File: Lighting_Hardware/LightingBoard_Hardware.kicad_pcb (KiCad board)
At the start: 2 copper layers, 61 x 108.8 mm, 22 parts, among them U1 LDD-1500L, U2 LDD-1500L, U3 TM4C129E_Launchpad, U4 OKI

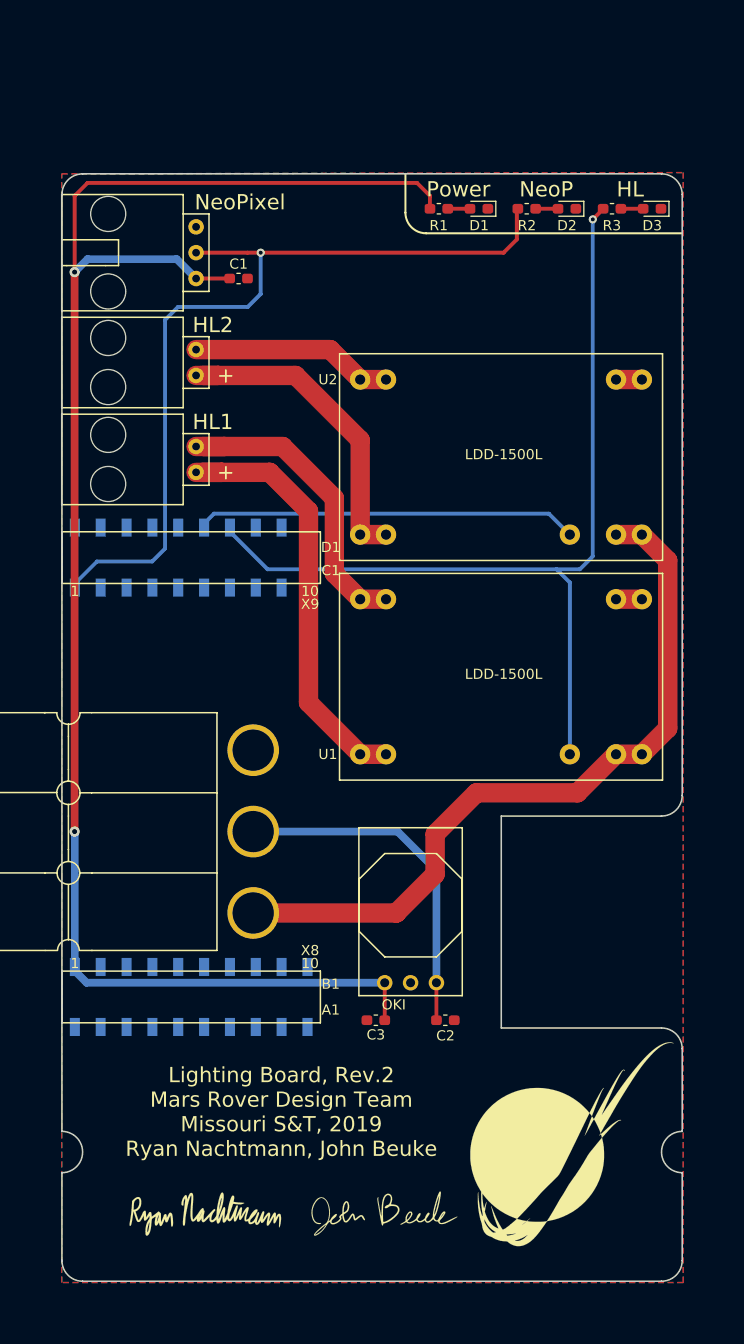
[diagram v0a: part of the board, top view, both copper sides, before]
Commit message: Added the NEW DC-DC Buck Converter for the NeoPixels
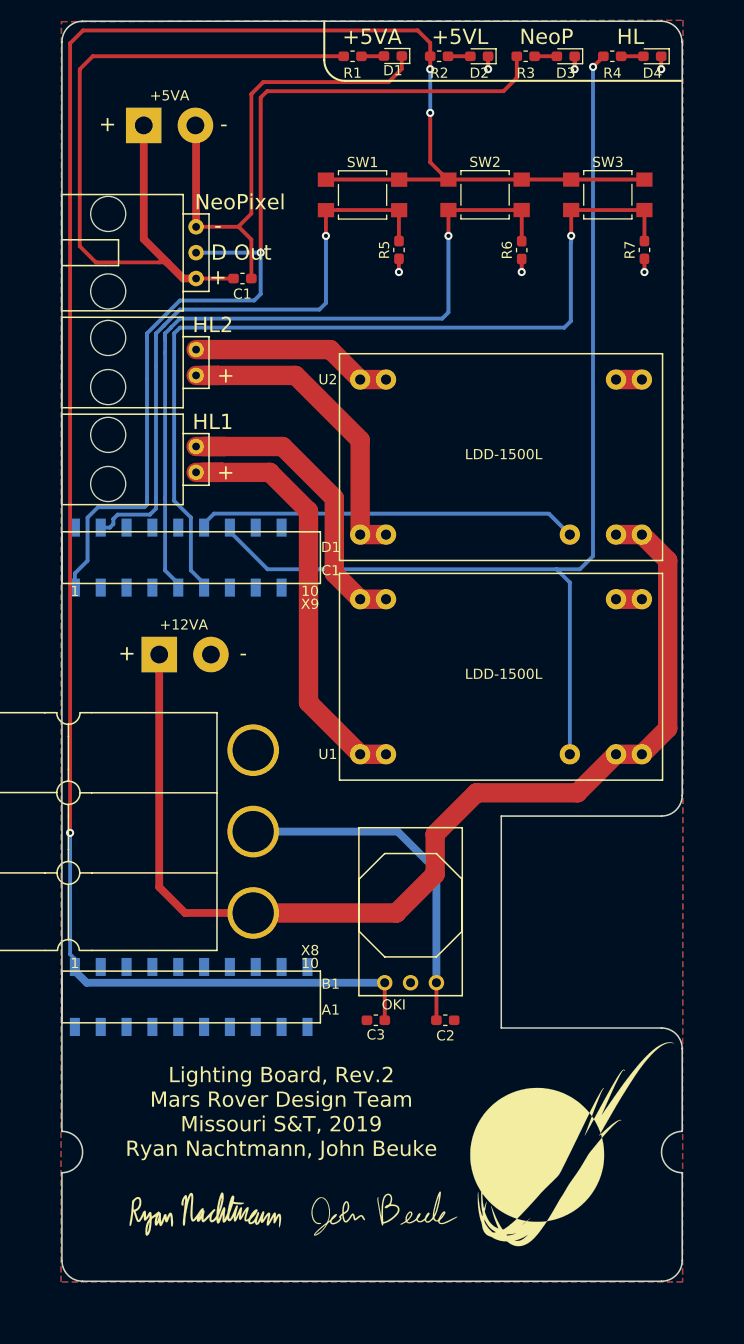
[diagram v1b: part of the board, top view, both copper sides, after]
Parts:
- added +12VA: SolderWirePad_1x02_P5.08mm_Drill1.5mm, Connector_Wire:SolderWirePad_1x02_P5.08mm_Drill1.5mm, F.Cu at (111.1, 87.4)
- added +5VA: SolderWirePad_1x02_P5.08mm_Drill1.5mm, Connector_Wire:SolderWirePad_1x02_P5.08mm_Drill1.5mm, F.Cu at (109.5, 35.4)
- added D4: Org_LED, LED_SMD:LED_0603_1608Metric_Pad1.05x0.95mm_HandSolder, F.Cu at (159.5, 28.6)
- added R4: 500, Resistor_SMD:R_0603_1608Metric_Pad1.05x0.95mm_HandSolder, F.Cu at (155.6, 28.6)
- added R5: 10K, Resistor_SMD:R_0603_1608Metric_Pad1.05x0.95mm_HandSolder, F.Cu at (134.6, 47.6)
- added R6: 10K, Resistor_SMD:R_0603_1608Metric_Pad1.05x0.95mm_HandSolder, F.Cu at (146.7, 47.6)
- added R7: 10K, Resistor_SMD:R_0603_1608Metric_Pad1.05x0.95mm_HandSolder, F.Cu at (158.8, 47.6)
- added SW1: SW_Push, Button_Switch_SMD:SW_SPST_TL3305A, F.Cu at (131.0, 42.2)
- added SW2: SW_Push, Button_Switch_SMD:SW_SPST_TL3305A, F.Cu at (143.1, 42.2)
- added SW3: SW_Push, Button_Switch_SMD:SW_SPST_TL3305A, F.Cu at (155.2, 42.2)
- D2: value Org_LED -> G_LED
- moved D2 17.3 mm to (142.5, 28.6)
- moved R2 17.3 mm to (138.6, 28.6)
- moved D1 17.2 mm to (134.0, 28.5)
- moved D3 17.2 mm to (151.0, 28.6)
- moved R1 17.2 mm to (130.1, 28.6)
- moved R3 17.2 mm to (147.1, 28.6)
- moved C1 0.38 mm to (119.2, 50.4)
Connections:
- C1 pad 1: +5V -> +5VA
- C1 pad 2: GND -> GNDA
- C3 pad 1: +5V -> +5VL
- Conn4 pad 1: +5V -> +5VA
- Conn4 pad 3: GND -> GNDA
- D1 pad 1: GND -> GNDA
- R1 pad 1: +5V -> +5VA
- R2 pad 1: Dout_NeoPixel -> +5VL
- R3 pad 1: Headlight_OnOff_PWM1 -> Dout_NeoPixel
- U3 pad +5V: +5V -> +5VL
- U3 pad PL4: Net-(U3-PadPL4) -> NeoPixel_White
- U3 pad PL5: Net-(U3-PadPL5) -> NeoPixel_Pattern
- U3 pad PM3: Net-(U3-PadPM3) -> Headlight_Power
- U4 pad 3: +5V -> +5VL
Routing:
- net +5VL: track 0.00 -> 208.0 mm, vias 0 -> 3
- net +5V: track 164.6 -> 0.00 mm, vias 2 -> 0
- net NeoPixel_Pattern: track 0.00 -> 86.9 mm, vias 0 -> 1
- net NeoPixel_White: track 0.00 -> 75.1 mm, vias 0 -> 1
- net +5VA: track 0.00 -> 74.7 mm
- net Headlight_Power: track 0.00 -> 61.6 mm, vias 0 -> 1
- net GNDA: track 0.00 -> 51.1 mm
- net +12VA: track 73.2 -> 106.3 mm
- net Dout_NeoPixel: track 82.8 -> 98.1 mm
- net Headlight_OnOff_PWM1: track 91.4 -> 106.4 mm
- net GND: track 5.08 -> 12.8 mm, vias 0 -> 6
- net Net-(D4-Pad2): track 0.00 -> 2.16 mm
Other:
- board size 61 x 108.8 mm -> 61 x 123.8 mm
- board text added: "+5VA"
- board text added: "+5VL"
- board text added: "-"
- board text added: "D Out"
- board text removed: "Power"

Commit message: Finished Rev2
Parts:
- added G***: LOGO, MRDT_Silkscreens:R2, F.Cu at (140.5, 32.6)
- U3: footprint MRDT_Shields:TM4C129E_Launchpad_X9_SMD -> MRDT_Shields:TM4C129E_Launchpad_X9_SMD_BOTTOM
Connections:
- R4 pad 1: Headlight_OnOff_PWM1 -> Headlight_OnOff_PWM
- U1 pad 21: Headlight_OnOff_PWM1 -> Headlight_OnOff_PWM
- U2 pad 21: Headlight_OnOff_PWM2 -> Headlight_OnOff_PWM
- U3 pad PB3: Net-(U3-PadPB3) -> Headlight_OnOff_PWM
- U3 pad PD0: Headlight_OnOff_PWM1 -> Net-(U3-PadPD0)
- U3 pad PD1: Headlight_OnOff_PWM2 -> Net-(U3-PadPD1)
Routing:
- net Headlight_OnOff_PWM: track 0.00 -> 124.5 mm, vias 0 -> 1
- net Headlight_OnOff_PWM1: track 106.4 -> 0.00 mm, vias 1 -> 0
- net Headlight_OnOff_PWM2: track 38.2 -> 0.00 mm
- net +5VA: track 74.7 -> 80.2 mm
- net +12VA: track 106.3 -> 109.9 mm
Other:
- board text added: "5V 8A Buck Converter"
- board text added: "Manual Control"
- board text added: "Pattern"
- board text added: "White"

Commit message: Regenerated Gerbs
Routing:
- net GND: vias 6 -> 13
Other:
- board text added: "ACT"
- board text added: "GND"
- board text added: "LOG"
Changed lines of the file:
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@@
   (general
     (thickness 1.6)
-    (drawings 57)
-    (tracks 227)
+    (drawings 61)
+    (tracks 234)
     (zones 0)
     (modules 33)
@@
     (47 F.CrtYd user)
     (48 B.Fab user)
-    (49 F.Fab user)
+    (49 F.Fab user hide)
   )
   (setup
-    (last_trace_width 0.381)
+    (last_trace_width 0.25)
     (user_trace_width 0.0381)
     (user_trace_width 0.03998)
@@
   (module MRDT_Devices:LDD-1500L_LED_DRIVER (layer F.Cu)
     (at 128.778 57.809 270)
-    (fp_text reference U2 (at 2.54 1.143) (layer B.Fab)
+    (fp_text reference U2 (at 4.802 1.27) (layer F.SilkS)
       (effects (font (size 1 1) (thickness 0.15)))
     )
@@
   (module MRDT_Devices:LDD-1500L_LED_DRIVER (layer F.Cu)
     (at 128.778 79.399 270)
-    (fp_text reference U1 (at 17.78 1.143) (layer B.Fab)
+    (fp_text reference U1 (at 4.929 1.143) (layer F.SilkS)
       (effects (font (size 1 1) (thickness 0.15)))
     )
@@
       (effects (font (size 1 1) (thickness 0.15)))
     )
-    (fp_text value OKI (at 6.731 -0.889 180) (layer F.SilkS)
+    (fp_text value OKI (at 4.953 8.89 180) (layer F.SilkS)
       (effects (font (size 1 1) (thickness 0.15)))
     )
@@
     (tags "resistor handsolder")
     (attr smd)
-    (fp_text reference R1 (at 0 1.651) (layer F.SilkS)
+    (fp_text reference R1 (at -0.0114 1.524) (layer F.SilkS)
       (effects (font (size 1 1) (thickness 0.15)))
     )
@@
     (tags "LED handsolder")
     (attr smd)
-    (fp_text reference D1 (at 0 -1.43 180) (layer F.SilkS)
+    (fp_text reference D1 (at 0.0368 -1.5494 180) (layer F.SilkS)
       (effects (font (size 1 1) (thickness 0.15)))
     )
@@
       (xy -0.187794 -0.475552) (xy -0.096549 -0.47895) (xy -0.000789 -0.479937) (xy 0.095818 -0.478557)) (layer F.SilkS) (width 0.01))
   )
+  (gr_text GND (at 125.095 96.774) (layer F.SilkS)
+    (effects (font (size 1.016 1.016) (thickness 0.254)))
+  )
+  (gr_text ACT (at 124.968 112.776) (layer F.SilkS)
+    (effects (font (size 1.016 1.016) (thickness 0.254)))
+  )
+  (gr_text LOG (at 124.968 104.775) (layer F.SilkS)
+    (effects (font (size 1.016 1.016) (thickness 0.254)))
+  )
+  (gr_text +5VL (at 135.636 103.124) (layer F.SilkS)
+    (effects (font (size 1.5 1.5) (thickness 0.3)))
+  )
   (gr_text "5V 8A Buck Converter" (at 139.3825 43.18) (layer B.SilkS)
     (effects (font (size 1.5 1.5) (thickness 0.3)) (justify mirror))
@@
   (segment (start 143.383 29.845) (end 143.383 29.845) (width 0.381) (layer F.Cu) (net 1))
   (via (at 143.383 29.845) (size 0.8) (drill 0.4) (layers F.Cu B.Cu) (net 1))
+  (via (at 103.632 68.072) (size 0.8) (drill 0.4) (layers F.Cu B.Cu) (net 1))
+  (via (at 103.632 63.373) (size 0.8) (drill 0.4) (layers F.Cu B.Cu) (net 1))
+  (via (at 103.505 72.009) (size 0.8) (drill 0.4) (layers F.Cu B.Cu) (net 1))
+  (via (at 134.62 50.8) (size 0.8) (drill 0.4) (layers F.Cu B.Cu) (net 1))
+  (via (at 146.685 50.8) (size 0.8) (drill 0.4) (layers F.Cu B.Cu) (net 1))
+  (via (at 158.75 50.8) (size 0.8) (drill 0.4) (layers F.Cu B.Cu) (net 1))
+  (via (at 103.632 58.547) (size 0.8) (drill 0.4) (layers F.Cu B.Cu) (net 1))
   (segment (start 138.303 123.317) (end 138.303 119.634) (width 0.381) (layer F.Cu) (net 2))
   (segment (start 138.303 119.634) (end 138.303 108.585) (width 0.762) (layer B.Cu) (net 2))
@@
   (segment (start 120.396 52.578) (end 121.031 51.943) (width 0.381) (layer B.Cu) (net 8))
   (segment (start 121.031 51.943) (end 121.031 47.879) (width 0.381) (layer B.Cu) (net 8))
-  (segment (start 118.008001 74.903601) (end 118.008001 75.297301) (width 0.381) (layer B.Cu) (net 50))
-  (segment (start 153.6954 29.619) (end 153.6954 29.619) (width 0.25) (layer F.Cu) (net 49))
-  (segment (start 154.7394 28.575) (end 153.6954 29.619) (width 0.381) (layer F.Cu) (net 49))
-  (segment (start 153.6954 29.619) (end 153.6954 29.619) (width 0.25) (layer F.Cu) (net 49))
-  (via (at 153.6954 29.619) (size 0.8) (drill 0.4) (layers F.Cu B.Cu) (net 49))
   (segment (start 130.9344 28.575) (end 133.1494 28.575) (width 0.381) (layer F.Cu) (net 39))
   (segment (start 139.4434 28.575) (end 141.6304 28.575) (width 0.381) (layer F.Cu) (net 40))
@@
   (segment (start 150.876 55.245) (end 113.0935 55.245) (width 0.381) (layer B.Cu) (net 48))
   (segment (start 113.0935 55.245) (end 112.522 55.8165) (width 0.381) (layer B.Cu) (net 48))
+  (segment (start 153.6954 29.619) (end 153.6954 29.619) (width 0.25) (layer F.Cu) (net 49))
+  (segment (start 154.7394 28.575) (end 153.6954 29.619) (width 0.381) (layer F.Cu) (net 49))
+  (segment (start 153.6954 29.619) (end 153.6954 29.619) (width 0.25) (layer F.Cu) (net 49))
+  (via (at 153.6954 29.619) (size 0.8) (drill 0.4) (layers F.Cu B.Cu) (net 49))
   (segment (start 125.628001 124.370101) (end 126.9879 125.73) (width 0.381) (layer B.Cu) (net 49))
   (segment (start 125.628001 123.976401) (end 125.628001 124.370101) (width 0.381) (layer B.Cu) (net 49))
@@
   (segment (start 153.6954 29.619) (end 153.6954 74.3966) (width 0.381) (layer B.Cu) (net 49))
   (segment (start 153.6954 74.3966) (end 152.503 75.589) (width 0.381) (layer B.Cu) (net 49))
+  (segment (start 118.008001 74.903601) (end 118.008001 75.297301) (width 0.381) (layer B.Cu) (net 50))
   (zone (net 1) (net_name GND) (layer B.Cu) (hatch edge 0.508)
     (connect_pads yes (clearance 0.508))
